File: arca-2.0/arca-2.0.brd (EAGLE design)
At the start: 405.1 x 101.6 mm, 169 parts, among them IC1 MCP6N11R, IC2 MCP6N11R, IC3 MCP6N11R, IC4 MCP6N11R, IC5 LM324D, IC6 LM324D, SW1 1101M2S3CQE2, T1 FQP30N06L, T2 FQP30N06L, T3 FQP30N06L, T4 FQP30N06L, T5 FQP30N06L, T6 FQP30N06L

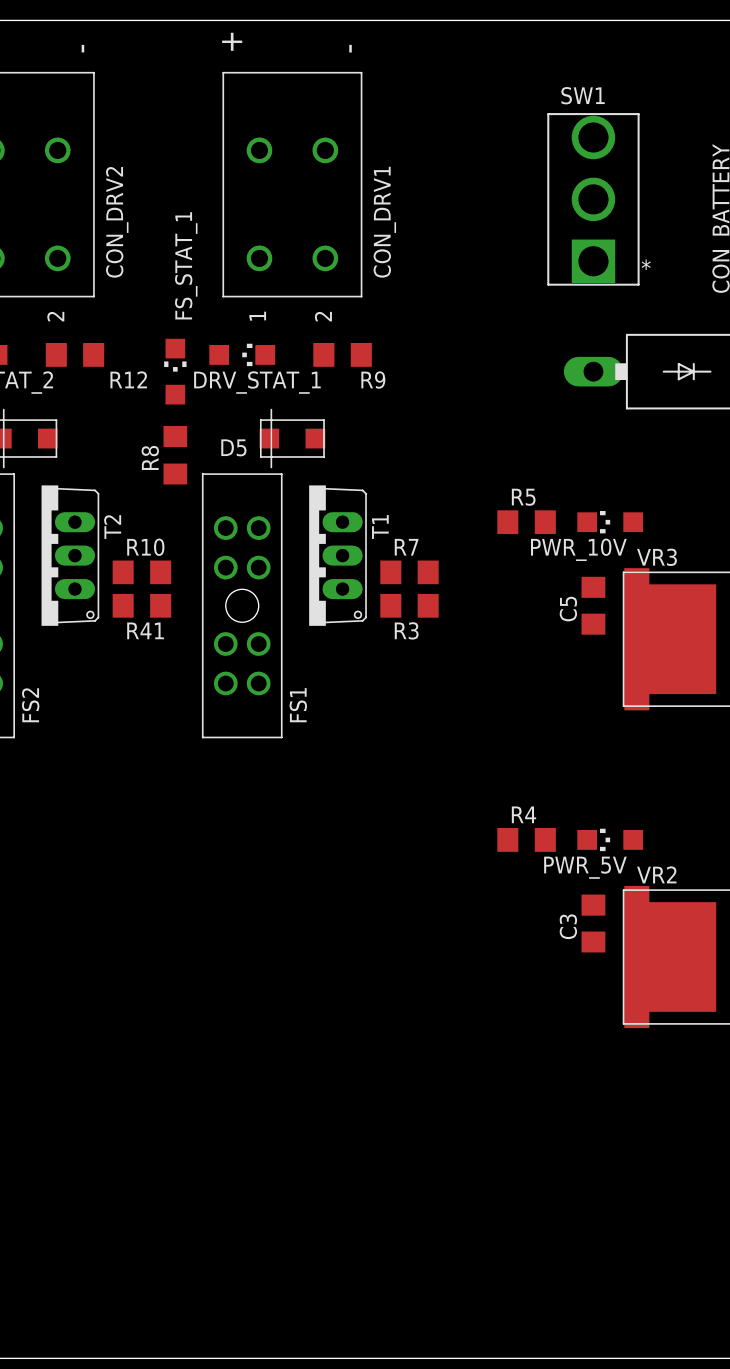
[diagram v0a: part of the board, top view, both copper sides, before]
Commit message: updating board with results from data analysis
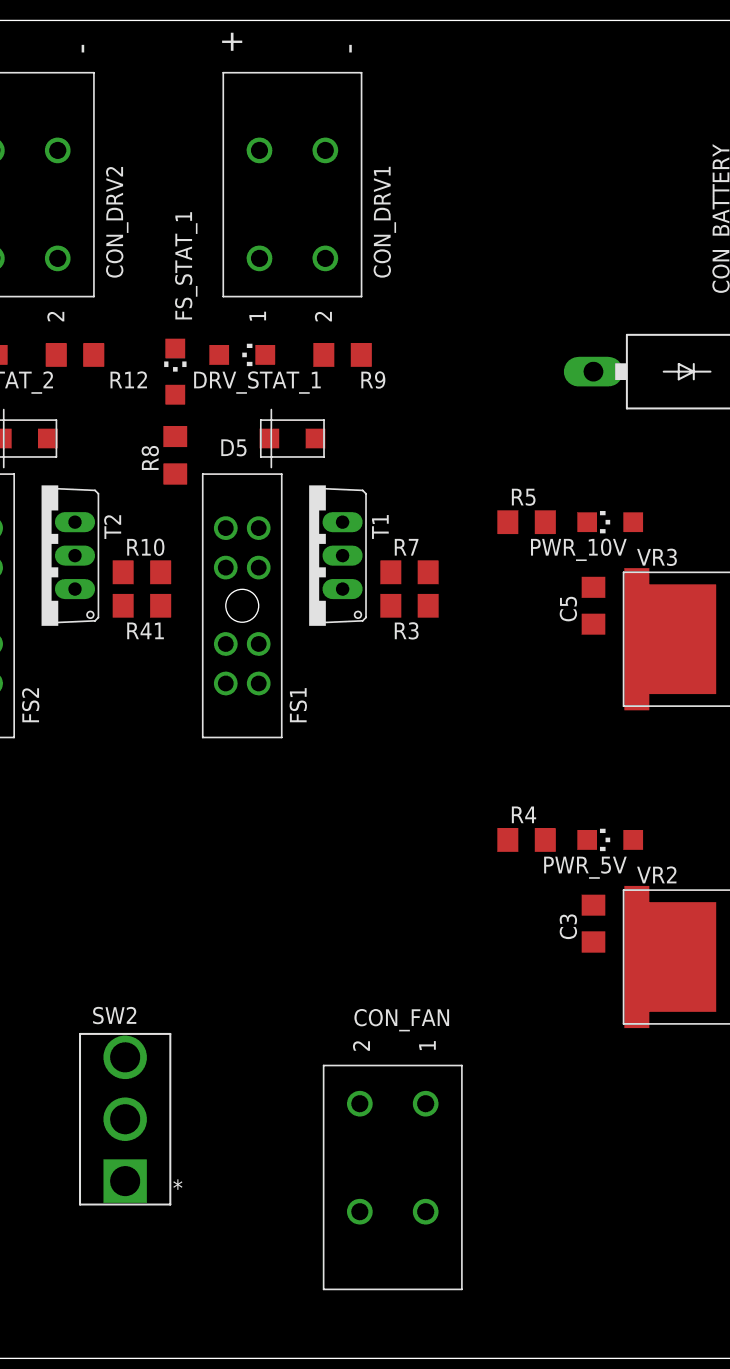
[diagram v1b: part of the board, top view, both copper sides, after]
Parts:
- removed SW1: 1101M2S3CQE2, switch-slide:1101M2S3CQE2
- added CON_FAN: LPTA-2POS, con-phoenix-5mm:8.2X2
- added SW2: 1101M2S3CQE2, switch-slide:1101M2S3CQE2
- C1, C2, C21, C22, C23, C24, C25, C26: value (none) -> 1n
- R25, R29, R33, R37: value 39k -> 15k
- R27, R28: value 56k -> 68k
- R31, R32, R35, R36, R39, R40: value 62k -> 68k
- R55, R56, R58, R59, R61, R62, R64, R65: value (none) -> 68k
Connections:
- new net N$48: CON_FAN.1, CON_FAN.2, SW2.1
- net +12V: now also SW2.2
- net 12V_CON: no longer SW1.2
- net 12V_IN: no longer SW1.1
- net GND: now also CON_FAN.3, CON_FAN.4

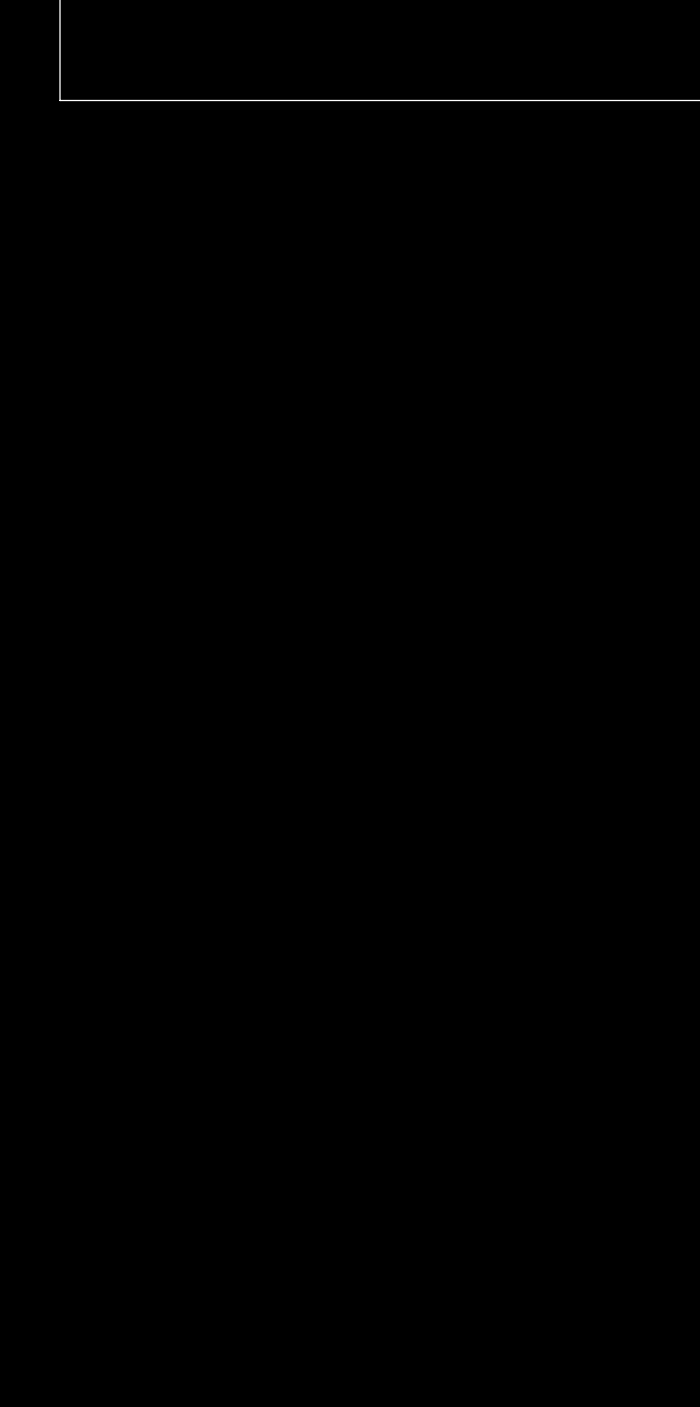
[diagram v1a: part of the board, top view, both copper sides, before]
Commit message: ADCs now added
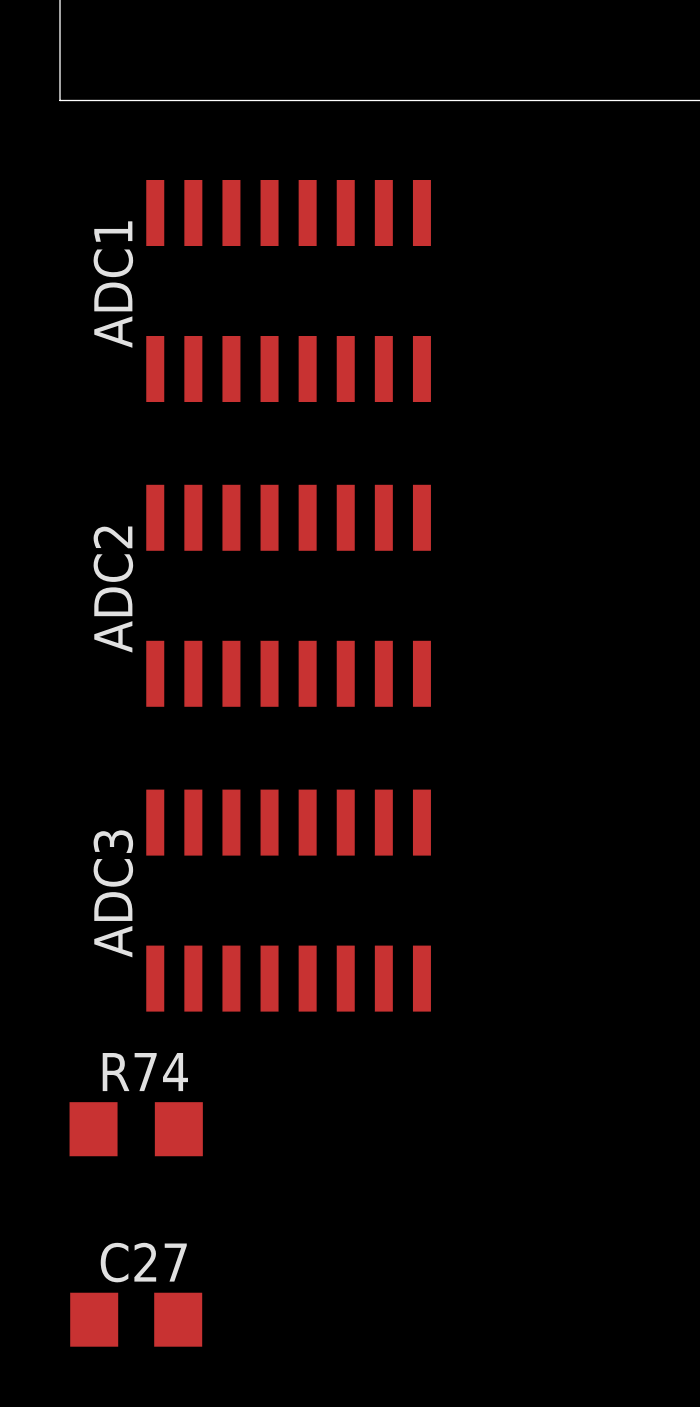
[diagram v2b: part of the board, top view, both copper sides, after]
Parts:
- added ADC1, ADC2, ADC3: MCP3208SN, microchip-extra:SO-16
- added C27: 0.1u, rcl:C1206
- added R74: 10k, rcl:R1206
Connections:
- new net N$49: ADC1.10, R74.2
- new net SPI_CLK: ADC1.13
- new net SPI_MISO: ADC1.12
- new net SPI_MOSI: ADC1.11
- net +5V: now also ADC1.15, ADC1.16, C27.1
- net GND: now also ADC1.14, ADC1.9, C27.2, R74.1
- net LC1_CAL: now also ADC1.1
- net LC2_CAL: now also ADC1.2
- net LC3_CAL: now also ADC1.3
- net LC4_CAL: now also ADC1.4
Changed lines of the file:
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@@
 <attribute name="VENDOR" value="C&amp;K" x="302.26" y="5.08" size="1.778" layer="27" rot="R180" display="off"/>
+</element>
+<element name="ADC1" library="microchip-extra" package="SO-16" value="MCP3208SN" x="7.62" y="-6.35" smashed="yes">
+<attribute name="MF" value="MICROCHIP" x="7.62" y="-6.35" size="1.778" layer="27" display="off"/>
+<attribute name="MPN" value="MCP3202-CI/SN" x="7.62" y="-6.35" size="1.778" layer="27" display="off"/>
+<attribute name="NAME" x="2.413" y="-8.255" size="1.27" layer="25" rot="R90"/>
+<attribute name="OC_FARNELL" value="1196803" x="7.62" y="-6.35" size="1.778" layer="27" display="off"/>
+<attribute name="OC_NEWARK" value="19C7207" x="7.62" y="-6.35" size="1.778" layer="27" display="off"/>
+<attribute name="VALUE" x="14.097" y="-8.255" size="1.27" layer="27" rot="R90"/>
+</element>
+<element name="ADC2" library="microchip-extra" package="SO-16" value="MCP3208SN" x="7.62" y="-16.51" smashed="yes">
+<attribute name="MF" value="MICROCHIP" x="7.62" y="-16.51" size="1.778" layer="27" display="off"/>
+<attribute name="MPN" value="MCP3202-CI/SN" x="7.62" y="-16.51" size="1.778" layer="27" display="off"/>
+<attribute name="NAME" x="2.413" y="-18.415" size="1.27" layer="25" rot="R90"/>
+<attribute name="OC_FARNELL" value="1196803" x="7.62" y="-16.51" size="1.778" layer="27" display="off"/>
+<attribute name="OC_NEWARK" value="19C7207" x="7.62" y="-16.51" size="1.778" layer="27" display="off"/>
+<attribute name="VALUE" x="14.097" y="-18.415" size="1.27" layer="27" rot="R90"/>
+</element>
+<element name="ADC3" library="microchip-extra" package="SO-16" value="MCP3208SN" x="7.62" y="-26.67" smashed="yes">
+<attribute name="MF" value="MICROCHIP" x="7.62" y="-26.67" size="1.778" layer="27" display="off"/>
+<attribute name="MPN" value="MCP3202-CI/SN" x="7.62" y="-26.67" size="1.778" layer="27" display="off"/>
+<attribute name="NAME" x="2.413" y="-28.575" size="1.27" layer="25" rot="R90"/>
+<attribute name="OC_FARNELL" value="1196803" x="7.62" y="-26.67" size="1.778" layer="27" display="off"/>
+<attribute name="OC_NEWARK" value="19C7207" x="7.62" y="-26.67" size="1.778" layer="27" display="off"/>
+<attribute name="VALUE" x="14.097" y="-28.575" size="1.27" layer="27" rot="R90"/>
+</element>
+<element name="R74" library="rcl" library_urn="urn:adsk.eagle:library:334" package="R1206" package3d_urn="urn:adsk.eagle:package:23540/2" value="10k" x="2.54" y="-34.29" smashed="yes">
+<attribute name="NAME" x="1.27" y="-33.02" size="1.27" layer="25"/>
+<attribute name="POPULARITY" value="19" x="2.54" y="-34.29" size="1.778" layer="27" display="off"/>
+<attribute name="SPICEPREFIX" value="R" x="2.54" y="-34.29" size="1.778" layer="27" display="off"/>
+<attribute name="VALUE" x="1.27" y="-36.83" size="1.27" layer="27"/>
+</element>
+<element name="C27" library="rcl" library_urn="urn:adsk.eagle:library:334" package="C1206" package3d_urn="urn:adsk.eagle:package:23618/2" value="0.1u" x="2.54" y="-40.64" smashed="yes">
+<attribute name="NAME" x="1.27" y="-39.37" size="1.27" layer="25"/>
+<attribute name="POPULARITY" value="24" x="2.54" y="-40.64" size="1.778" layer="27" display="off"/>
+<attribute name="SPICEPREFIX" value="C" x="2.54" y="-40.64" size="1.778" layer="27" display="off"/>
+<attribute name="VALUE" x="1.27" y="-43.18" size="1.27" layer="27"/>
 </element>
 </elements>
@@
 <contactref element="FS8" pad="8"/>
 <contactref element="FS8" pad="6"/>
+<contactref element="ADC1" pad="15"/>
+<contactref element="ADC1" pad="16"/>
+<contactref element="C27" pad="1"/>
 <wire x1="168.93" y1="61.87" x2="171.43" y2="61.87" width="0" layer="19" extent="1-1"/>
 <wire x1="171.43" y1="58.87" x2="171.43" y2="61.87" width="0" layer="19" extent="1-1"/>
@@
 <wire x1="345.44" y1="30.48" x2="342.42" y2="38.1" width="0" layer="19" extent="1-1"/>
 <wire x1="247.65" y1="28.092" x2="255.422" y2="57.15" width="0" layer="19" extent="1-1"/>
+<wire x1="4.445" y1="-3.75" x2="47.05" y2="44.45" width="0" layer="19" extent="1-1"/>
+<wire x1="3.175" y1="-3.75" x2="4.445" y2="-3.75" width="0" layer="19" extent="1-1"/>
+<wire x1="1.14" y1="-40.64" x2="3.175" y2="-3.75" width="0" layer="19" extent="1-1"/>
 </signal>
 <signal name="GND">
@@
 <contactref element="CON_FAN" pad="3"/>
 <contactref element="CON_FAN" pad="4"/>
+<contactref element="ADC1" pad="14"/>
+<contactref element="R74" pad="1"/>
+<contactref element="ADC1" pad="9"/>
+<contactref element="C27" pad="2"/>
 <wire x1="168.79" y1="89.19" x2="168.79" y2="80.99" width="0" layer="19" extent="1-1"/>
 <wire x1="159.385" y1="71.18" x2="168.79" y2="80.99" width="0" layer="19" extent="1-1"/>
@@
 <wire x1="35.56" y1="26.518" x2="31.62" y2="40.64" width="0" layer="19" extent="1-1"/>
 <wire x1="16.51" y1="68.428" x2="34.29" y2="62.382" width="0" layer="19" extent="1-1"/>
+<wire x1="12.065" y1="-3.75" x2="35.56" y2="26.518" width="0" layer="19" extent="1-1"/>
+<wire x1="5.715" y1="-3.75" x2="12.065" y2="-3.75" width="0" layer="19" extent="1-1"/>
+<wire x1="1.118" y1="-34.29" x2="5.715" y2="-3.75" width="0" layer="19" extent="1-1"/>
+<wire x1="3.94" y1="-40.64" x2="1.118" y2="-34.29" width="0" layer="19" extent="1-1"/>
 <wire x1="215.9" y1="67.158" x2="168.79" y2="80.99" width="0" layer="19" extent="1-1"/>
 <wire x1="228.6" y1="63.5" x2="215.9" y2="67.158" width="0" layer="19" extent="1-1"/>
@@
 <contactref element="R25" pad="2"/>
 <contactref element="C12" pad="2"/>
+<contactref element="ADC1" pad="1"/>
 <wire x1="133.22" y1="25.4" x2="132.14" y2="30.48" width="0" layer="19" extent="1-1"/>
 <wire x1="133.198" y1="22.86" x2="133.22" y2="25.4" width="0" layer="19" extent="1-1"/>
+<wire x1="3.175" y1="-8.95" x2="133.198" y2="22.86" width="0" layer="19" extent="1-1"/>
 </signal>
 <signal name="N$31">
@@
 <contactref element="C14" pad="2"/>
 <contactref element="IC5" pad="7"/>
+<contactref element="ADC1" pad="2"/>
 <wire x1="133.22" y1="43.18" x2="133.198" y2="45.72" width="0" layer="19" extent="1-1"/>
 <wire x1="132.14" y1="38.1" x2="133.22" y2="43.18" width="0" layer="19" extent="1-1"/>
+<wire x1="4.445" y1="-8.95" x2="132.14" y2="38.1" width="0" layer="19" extent="1-1"/>
 </signal>
 <signal name="+5V_FS" class="3">
@@
 <contactref element="C16" pad="2"/>
 <contactref element="IC5" pad="8"/>
+<contactref element="ADC1" pad="3"/>
 <wire x1="125.86" y1="43.18" x2="125.882" y2="45.72" width="0" layer="19" extent="1-1"/>
 <wire x1="126.94" y1="38.1" x2="125.86" y2="43.18" width="0" layer="19" extent="1-1"/>
+<wire x1="5.715" y1="-8.95" x2="126.94" y2="38.1" width="0" layer="19" extent="1-1"/>
 </signal>
 <signal name="LC4_CAL">
@@
 <contactref element="C18" pad="2"/>
 <contactref element="IC5" pad="14"/>
+<contactref element="ADC1" pad="4"/>
 <wire x1="125.86" y1="25.4" x2="126.94" y2="30.48" width="0" layer="19" extent="1-1"/>
 <wire x1="125.882" y1="22.86" x2="125.86" y2="25.4" width="0" layer="19" extent="1-1"/>
+<wire x1="6.985" y1="-8.95" x2="125.882" y2="22.86" width="0" layer="19" extent="1-1"/>
 </signal>
 <signal name="N$2">
@@
 <wire x1="293.37" y1="13.462" x2="316.19" y2="11.14" width="0" layer="19" extent="1-1"/>
 </signal>
+<signal name="SPI_CLK">
+<contactref element="ADC1" pad="13"/>
+</signal>
+<signal name="N$49">
+<contactref element="ADC1" pad="10"/>
+<contactref element="R74" pad="2"/>
+<wire x1="10.795" y1="-3.75" x2="3.962" y2="-34.29" width="0" layer="19" extent="1-1"/>
+</signal>
+<signal name="SPI_MISO">
+<contactref element="ADC1" pad="12"/>
+</signal>
+<signal name="SPI_MOSI">
+<contactref element="ADC1" pad="11"/>
+</signal>
 </signals>

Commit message: raspberry pi pinouts
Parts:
- added C28, C29: 0.1u, rcl:C1206
- added CON_TC1, CON_TC2, CON_TC3, CON_TC4: LPTA-4POS, con-phoenix-5mm:8.2X4
- added JP1, JP2, JP3, JP5, JP7: (no value), pinhead:1X08
- added JP4, JP6: (no value), pinhead:1X04
- added R75, R76: 10k, rcl:R1206
- added SW1: 1101M2S3CQE2, switch-slide:1101M2S3CQE2
- added X1: 2540-5, con-3m:PAK100/2500-5-40
- moved ADC1 228.0 mm to (207.0, 104.1), turned to 180 degrees
- moved R74 138.1 mm to (80.0, 80.0), turned to 180 degrees
- moved C27 136.0 mm to (80.0, 71.1), turned to 180 degrees
- moved ADC2 123.3 mm to (88.9, 76.2), turned to 90 degrees
- moved ADC3 94.4 mm to (39.4, 62.2), turned to 180 degrees
- moved FS8 79.3 mm to (234.9, 110.5)
- moved CON_DRV6 66.3 mm to (283.2, 11.4), turned to 90 degrees
- moved FS1 62.0 mm to (344.2, 102.9)
- moved FS2 62.0 mm to (323.9, 102.9)
- moved R3 62.0 mm to (356.9, 102.9)
- moved R41 62.0 mm to (336.6, 102.9)
- moved R42 62.0 mm to (316.2, 102.9)
- moved R43 62.0 mm to (295.9, 102.9)
- moved T1 62.0 mm to (349.2, 106.7)
- moved T2 62.0 mm to (328.9, 106.7)
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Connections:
- new net ADC1_CS: ADC1.10, R76.1, X1.26
- new net ADC2_CS: ADC2.10, R74.1, X1.24
- new net ADC3_CS: ADC3.10, R75.1, X1.22
- new net N$50: ADC1.6, JP1.6
- new net N$51: ADC1.7, JP1.7
- new net N$52: ADC1.8, JP1.8
- new net N$53: ADC2.8, JP2.8
- new net N$54: ADC2.7, JP2.7
- new net N$55: ADC2.6, JP2.6
- new net N$56: ADC2.5, JP2.5
- new net N$57: ADC3.5, JP3.5
- new net N$58: ADC3.6, JP3.6
- new net N$59: ADC3.7, JP3.7
- new net N$60: ADC3.8, JP3.8
- new net N$67: JP7.7
- new net N$68: JP7.8
- new net TC1: ADC1.1, CON_TC1.3, CON_TC1.4, JP1.1
- new net TC2: ADC1.2, CON_TC2.3, CON_TC2.4, JP1.2
- new net TC3: ADC1.3, CON_TC3.3, CON_TC3.4, JP1.3
- new net TC4: ADC1.4, CON_TC4.3, CON_TC4.4, JP1.4
- net +5V: now also ADC2.15, ADC2.16, ADC3.15, ADC3.16, C28.1, C29.1, R74.2, R75.2, R76.2, X1.2, X1.4
- net +5V_FS: now also CON_TC1.1, CON_TC1.2, CON_TC2.1, CON_TC2.2, CON_TC3.1, CON_TC3.2, CON_TC4.1, CON_TC4.2
- net 12V_CON: now also SW1.2
- net 12V_IN: now also SW1.1
- net DRV_CTL_1: now also JP7.1, X1.11
- net DRV_CTL_2: now also JP7.2, X1.13
- net DRV_CTL_3: now also JP7.3, X1.15
- net DRV_CTL_4: now also JP7.4, X1.18
- net DRV_CTL_5: now also JP7.5, X1.33
- net DRV_CTL_6: now also JP7.6, X1.32
- net GND: now also ADC2.14, ADC2.9, ADC3.14, ADC3.9, C28.2, C29.2, CON_TC1.7, CON_TC1.8, CON_TC2.7, CON_TC2.8, CON_TC3.7, CON_TC3.8, CON_TC4.7, CON_TC4.8, X1.14, X1.20, X1.25, X1.30, X1.34, X1.39, X1.6, X1.9; no longer R74.1
- net LC1+: now also JP5.1
- net LC1-: now also JP5.2
- net LC1_CAL: now also ADC2.1, JP2.1; no longer ADC1.1
- net LC1_PREC: now also JP6.1
- net LC2+: now also JP5.3
- net LC2-: now also JP5.4
- net LC2_CAL: now also ADC2.2, JP2.2; no longer ADC1.2
- net LC2_PREC: now also JP6.2
- net LC3+: now also JP5.5
- net LC3-: now also JP5.6
- net LC3_CAL: now also ADC2.3, JP2.3; no longer ADC1.3
- net LC3_PREC: now also JP6.3
- net LC4+: now also JP5.7
- net LC4-: now also JP5.8
- net LC4_CAL: now also ADC2.4, JP2.4; no longer ADC1.4
- net LC4_PREC: now also JP6.4
- net N$49: now also ADC1.5, JP1.5; no longer ADC1.10, R74.2
- net PT1-: now also JP4.1
- net PT1_CAL: now also ADC3.1, JP3.1
- net PT2-: now also JP4.2
- net PT2_CAL: now also ADC3.2, JP3.2
- net PT3-: now also JP4.3
- net PT3_CAL: now also ADC3.3, JP3.3
- net PT4-: now also JP4.4
- net PT4_CAL: now also ADC3.4, JP3.4
- net SPI_CLK: now also ADC2.13, ADC3.13, X1.23
- net SPI_MISO: now also ADC2.12, ADC3.12, X1.21
- net SPI_MOSI: now also ADC2.11, ADC3.11, X1.19
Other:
- board size 405.1 x 101.6 mm -> 364.5 x 148.6 mm
- board text added: "+ -"
- board text added: "+5V VOUT GND"

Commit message: some preliminary routing - ready for autorouter?
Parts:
- moved R4 120.7 mm to (203.2, 33.0)
- moved R5 120.7 mm to (203.2, 57.1)
- moved R6 120.7 mm to (238.8, 53.3)
- moved C3 120.7 mm to (208.3, 26.7)
- moved C4 120.7 mm to (228.6, 25.4)
- moved C5 120.7 mm to (208.3, 50.8)
- moved C6 120.7 mm to (228.6, 49.5)
- moved D2 120.7 mm to (223.5, 31.8)
- moved D3 120.7 mm to (223.5, 55.9)
- moved R1 120.7 mm to (223.5, 40.6)
- moved R2 120.7 mm to (223.5, 38.1)
- moved VR2 120.7 mm to (224.8, 24.1)
- moved VR3 120.7 mm to (224.8, 48.3)
- moved PWR_10V 120.7 mm to (209.6, 57.1)
- moved PWR_12V 120.7 mm to (233.7, 57.1)
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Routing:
- net +5V: track 0.00 -> 52.9 mm
- net DRV_POS_3: track 0.00 -> 46.4 mm
- net DRV_POS_2: track 0.00 -> 46.4 mm
- net DRV_POS_5: track 0.00 -> 46.4 mm
- net DRV_POS_4: track 0.00 -> 46.4 mm
- net DRV_POS_1: track 0.00 -> 46.4 mm
- net DRV_POS_6: track 0.00 -> 45.0 mm
- net DRV_NEG_1: track 0.00 -> 36.1 mm
- net DRV_NEG_2: track 0.00 -> 35.7 mm
- net DRV_NEG_6: track 0.00 -> 35.2 mm
- net DRV_NEG_3: track 0.00 -> 35.0 mm
- net DRV_NEG_5: track 0.00 -> 34.8 mm
- net DRV_NEG_4: track 0.00 -> 34.1 mm
- net N$30: track 0.00 -> 17.6 mm
- net N$26: track 0.00 -> 17.5 mm
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- added copper zone on layer 1, net +10V
- added copper zone on layer 1, net +5V
- added copper zone on layer 1, net GND
- added copper zone on layer 16, net GND
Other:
- board size 364.5 x 148.6 mm -> 355.6 x 127 mm

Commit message: first rev of board
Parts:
- turned R17 to 90 degrees
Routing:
- net +5V: track 52.9 -> 685.0 mm, vias 0 -> 15
- net +12V: track 0.00 -> 329.3 mm, vias 0 -> 1
- net DRV_CTL_1: track 6.72 -> 303.5 mm
- net DRV_CTL_2: track 0.00 -> 279.3 mm, vias 0 -> 1
- net +5V_FS: track 0.00 -> 256.5 mm
- net DRV_CTL_3: track 6.72 -> 260.1 mm
- net DRV_CTL_6: track 6.72 -> 259.3 mm, vias 0 -> 1
- net DRV_CTL_4: track 6.72 -> 246.0 mm
- net SPI_MOSI: track 0.00 -> 215.1 mm
- net DRV_CTL_5: track 6.72 -> 218.9 mm
- net SPI_MISO: track 0.00 -> 210.3 mm, vias 0 -> 3
- net SPI_CLK: track 0.00 -> 207.7 mm, vias 0 -> 2
- net +10V: track 0.00 -> 166.8 mm, vias 0 -> 1
- net ADC1_CS: track 0.00 -> 124.5 mm
- net +10V_FS: track 0.00 -> 112.7 mm
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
